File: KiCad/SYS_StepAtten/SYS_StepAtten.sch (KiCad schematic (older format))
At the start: 125 parts, among them J1 RCA-1, J2 RCA-2, J3 AUX-1-2, J4 Barrel_Jack 9Vac, J5 POT_EXT Conn, J6 cfg jumper, J7 ARM SWD, J8 RCA-Out, K1 TQ2SA, K10 TQ2SA, K11 TQ2SA, K12 TQ2SA, K13 TQ2SA, K14 TQ2SA, K2 TQ2SA, K3 TQ2SA, K4 TQ2SA, K5 TQ2SA, K6 TQ2SA, K7 TQ2SA, K8 TQ2SA, K9 TQ2SA, Q1 2N7002, Q10 2N7002, Q11 2N7002, Q12 2N7002, Q13 2N7002, Q14 2N7002, Q2 2N7002, Q3 2N7002, Q4 2N7002, Q5 2N7002, Q6 2N7002, Q7 2N7002, Q8 2N7002, Q9 2N7002, SW1 ON/OFF, SW2 INPUT_SWITCH, U1 LM317, U2 STM32f030K6T6, U3 L7805, Y1 8Mhz

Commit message: Cleared Annotations, Will have to redo pcb anyway
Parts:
- renumbered C13 to C?, C12 to C?, C5 to C?, C6 to C?, C2 to C?, C3 to C?, C14 to C?, C4 to C?, C10 to C?, C11 to C?, C9 to C?, C8 to C?, C7 to C?, C1 to C?, D11 to D?, D9 to D?, D10 to D?, D1 to D?, D7 to D?, D8 to D?, D2 to D?, D6 to D?, D12 to D?, D13 to D?, D14 to D?, D15 to D?, D16 to D?, D17 to D?, D18 to D?, D19 to D?, D20 to D?, D21 to D?, D3 to D?, D4 to D?, D5 to D?, H1 to H?, H2 to H?, J7 to J?, J3 to J?, J4 to J?, J6 to J?, J1 to J?, J2 to J?, J8 to J?, J5 to J?, JP1 to JP?, JP2 to JP?, K1 to K?, K2 to K?, K3 to K?, K4 to K?, K5 to K?, K6 to K?, K7 to K?, K8 to K?, K9 to K?, K10 to K?, K11 to K?, K12 to K?, K13 to K?, K14 to K?, Q4 to Q?, Q2 to Q?, Q3 to Q?, Q1 to Q?, Q6 to Q?, Q5 to Q?, Q8 to Q?, Q7 to Q?, Q10 to Q?, Q9 to Q?, Q12 to Q?, Q11 to Q?, Q14 to Q?, Q13 to Q?, R10 to R?, R9 to R?, R7 to R?, R8 to R?, R14 to R?, R13 to R?, R11 to R?, R12 to R?, R19 to R?, R18 to R?, R16 to R?, R17 to R?, R23 to R?, R22 to R?, R20 to R?, R21 to R?, R27 to R?, R26 to R?, R24 to R?, R25 to R?, R31 to R?, R30 to R?, R28 to R?, R29 to R?, R35 to R?, R34 to R?, R32 to R?, R33 to R?, R37 to R?, R36 to R?, R38 to R?, R39 to R?, R40 to R?, R41 to R?, R5 to R?, R6 to R?, R15 to R?, R2 to R?, R3 to R?, R4 to R?, R1 to R?, RV1 to RV?, SW1 to SW?, SW2 to SW?, TP1 to TP?, TP2 to TP?, U3 to U?, U1 to U?, U2 to U?, Y1 to Y?

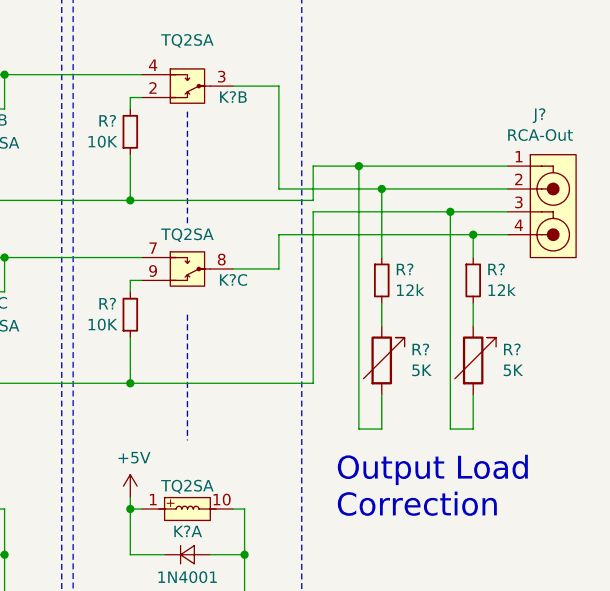
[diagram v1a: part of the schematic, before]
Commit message: Added Series Output Load Adjustment
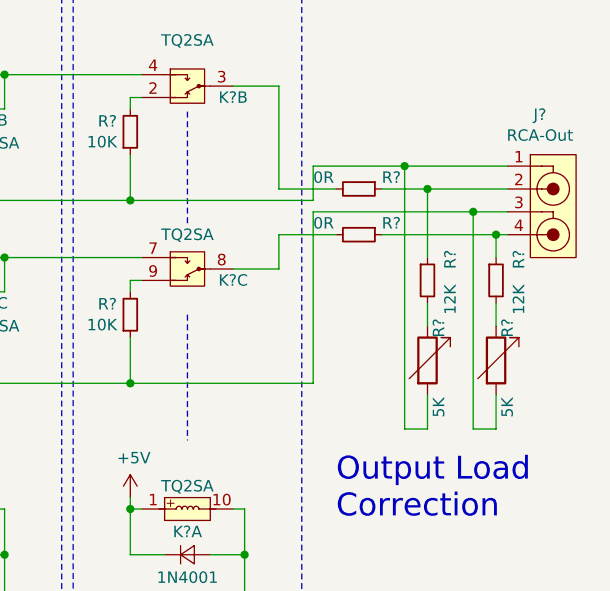
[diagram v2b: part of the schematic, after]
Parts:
- added R? (x2): 0R, Resistor_SMD:R_0603_1608Metric, symbol Device:R_Small
- R? (x2): value 12k -> 12K
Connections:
- net at J?.2, R?.1: now also R?.1; no longer K?.3
- net at J?.4, R?.1: now also R?.1; no longer K?.8
- new net: K?.8, R?.2
- new net: K?.3, R?.2
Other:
- moved on the sheet: R?
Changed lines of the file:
@@
 	1    0    0    -1
 $EndComp
-Wire Wire Line
-	14750 2450 15350 2450
-Wire Wire Line
-	14600 2550 15450 2550
 $Comp
 L Device:R_Small R?
 U 1 1 5F1C9E77
-P 15050 2750
-F 0 "R?" H 15109 2796 50  0000 L CNN
-F 1 "12k" H 15109 2705 50  0000 L CNN
-F 2 "Resistor_SMD:R_0603_1608Metric" H 15050 2750 50  0001 C CNN
-F 3 "~" H 15050 2750 50  0001 C CNN
-	1    15050 2750
+P 15250 2750
+F 0 "R?" V 15350 2800 50  0000 L CNN
+F 1 "12K" V 15350 2600 50  0000 L CNN
+F 2 "Resistor_SMD:R_0603_1608Metric" H 15250 2750 50  0001 C CNN
+F 3 "~" H 15250 2750 50  0001 C CNN
+	1    15250 2750
 	1    0    0    -1
 $EndComp
@@
 L Device:R_Variable R?
 U 1 1 5F1CB0BC
-P 15050 3100
-F 0 "R?" H 15178 3146 50  0000 L CNN
-F 1 "5K" H 15178 3055 50  0000 L CNN
-F 2 "Potentiometer_THT:Potentiometer_Bourns_3296W_Vertical" V 14980 3100 50  0001 C CNN
-F 3 "~" H 15050 3100 50  0001 C CNN
-	1    15050 3100
+P 15250 3100
+F 0 "R?" V 15300 3200 50  0000 L CNN
+F 1 "5K" V 15300 2850 50  0000 L CNN
+F 2 "Potentiometer_THT:Potentiometer_Bourns_3296W_Vertical" V 15180 3100 50  0001 C CNN
+F 3 "~" H 15250 3100 50  0001 C CNN
+	1    15250 3100
 	1    0    0    -1
 $EndComp
@@
 L Device:R_Small R?
 U 1 1 5F1CB5A8
-P 15450 2750
-F 0 "R?" H 15509 2796 50  0000 L CNN
-F 1 "12k" H 15509 2705 50  0000 L CNN
-F 2 "Resistor_SMD:R_0603_1608Metric" H 15450 2750 50  0001 C CNN
-F 3 "~" H 15450 2750 50  0001 C CNN
-	1    15450 2750
+P 15550 2750
+F 0 "R?" V 15650 2800 50  0000 L CNN
+F 1 "12K" V 15650 2600 50  0000 L CNN
+F 2 "Resistor_SMD:R_0603_1608Metric" H 15550 2750 50  0001 C CNN
+F 3 "~" H 15550 2750 50  0001 C CNN
+	1    15550 2750
 	1    0    0    -1
 $EndComp
@@
 L Device:R_Variable R?
 U 1 1 5F1F1DD1
-P 15450 3100
-F 0 "R?" H 15578 3146 50  0000 L CNN
-F 1 "5K" H 15578 3055 50  0000 L CNN
-F 2 "Potentiometer_THT:Potentiometer_Bourns_3296W_Vertical" V 15380 3100 50  0001 C CNN
-F 3 "~" H 15450 3100 50  0001 C CNN
-	1    15450 3100
+P 15550 3100
+F 0 "R?" V 15600 3200 50  0000 L CNN
+F 1 "5K" V 15600 2850 50  0000 L CNN
+F 2 "Potentiometer_THT:Potentiometer_Bourns_3296W_Vertical" V 15480 3100 50  0001 C CNN
+F 3 "~" H 15550 3100 50  0001 C CNN
+	1    15550 3100
 	1    0    0    -1
 $EndComp
 Wire Wire Line
-	15450 2950 15450 2850
-Wire Wire Line
-	15050 2850 15050 2950
-Wire Wire Line
-	15450 2650 15450 2550
-Connection ~ 15450 2550
+	15550 2950 15550 2850
 Wire Wire Line
-	15450 2550 15600 2550
+	15250 2850 15250 2950
 Wire Wire Line
-	15050 2650 15050 2350
+	15550 2650 15550 2550
 Wire Wire Line
-	15050 2350 15600 2350
+	15250 2650 15250 2350
 Wire Wire Line
-	15050 3250 15050 3400
+	15250 3250 15250 3400
 Wire Wire Line
-	15050 3400 14950 3400
+	15250 3400 15150 3400
 Wire Wire Line
-	14950 3400 14950 2250
+	15150 3400 15150 2250
 Wire Wire Line
-	14950 2250 15600 2250
+	15550 3250 15550 3400
 Wire Wire Line
-	15450 3250 15450 3400
+	15550 3400 15450 3400
 Wire Wire Line
-	15450 3400 15350 3400
-Wire Wire Line
-	15350 3400 15350 2450
-Connection ~ 15350 2450
-Wire Wire Line
-	15350 2450 15600 2450
+	15450 3400 15450 2450
 $Comp
 L Connector_Generic:Conn_02x05_Odd_Even J?
@@
 $EndComp
 Wire Wire Line
-	14750 2250 14950 2250
-Wire Wire Line
 	14750 2250 14750 2400
-Connection ~ 14950 2250
-Wire Wire Line
-	15050 2350 14600 2350
 Wire Wire Line
 	14600 1900 14600 2350
-Connection ~ 15050 2350
+$Comp
+L Device:R_Small R?
+U 1 1 5EF195F1
+P 14950 2550
+F 0 "R?" V 14900 2650 50  0000 L CNN
+F 1 "0R" V 14900 2350 50  0000 L CNN
+F 2 "Resistor_SMD:R_0603_1608Metric" H 14950 2550 50  0001 C CNN
+F 3 "~" H 14950 2550 50  0001 C CNN
+	1    14950 2550
+	0    1    1    0
+$EndComp
+$Comp
+L Device:R_Small R?
+U 1 1 5F00084E
+P 14950 2350
+F 0 "R?" V 14900 2450 50  0000 L CNN
+F 1 "0R" V 14900 2150 50  0000 L CNN
+F 2 "Resistor_SMD:R_0603_1608Metric" H 14950 2350 50  0001 C CNN
+F 3 "~" H 14950 2350 50  0001 C CNN
+	1    14950 2350
+	0    1    1    0
+$EndComp
+Wire Wire Line
+	14850 2350 14600 2350
+Wire Wire Line
+	15050 2350 15250 2350
+Wire Wire Line
+	15250 2350 15600 2350
+Connection ~ 15250 2350
+Wire Wire Line
+	15600 2250 15150 2250
+Wire Wire Line
+	15150 2250 14750 2250
+Connection ~ 15150 2250
+Wire Wire Line
+	15050 2550 15550 2550
+Wire Wire Line
+	15550 2550 15600 2550
+Connection ~ 15550 2550
+Wire Wire Line
+	15450 2450 15600 2450
+Wire Wire Line
+	15450 2450 14750 2450
+Connection ~ 15450 2450
+Wire Wire Line
+	14600 2550 14850 2550
 $EndSCHEMATC

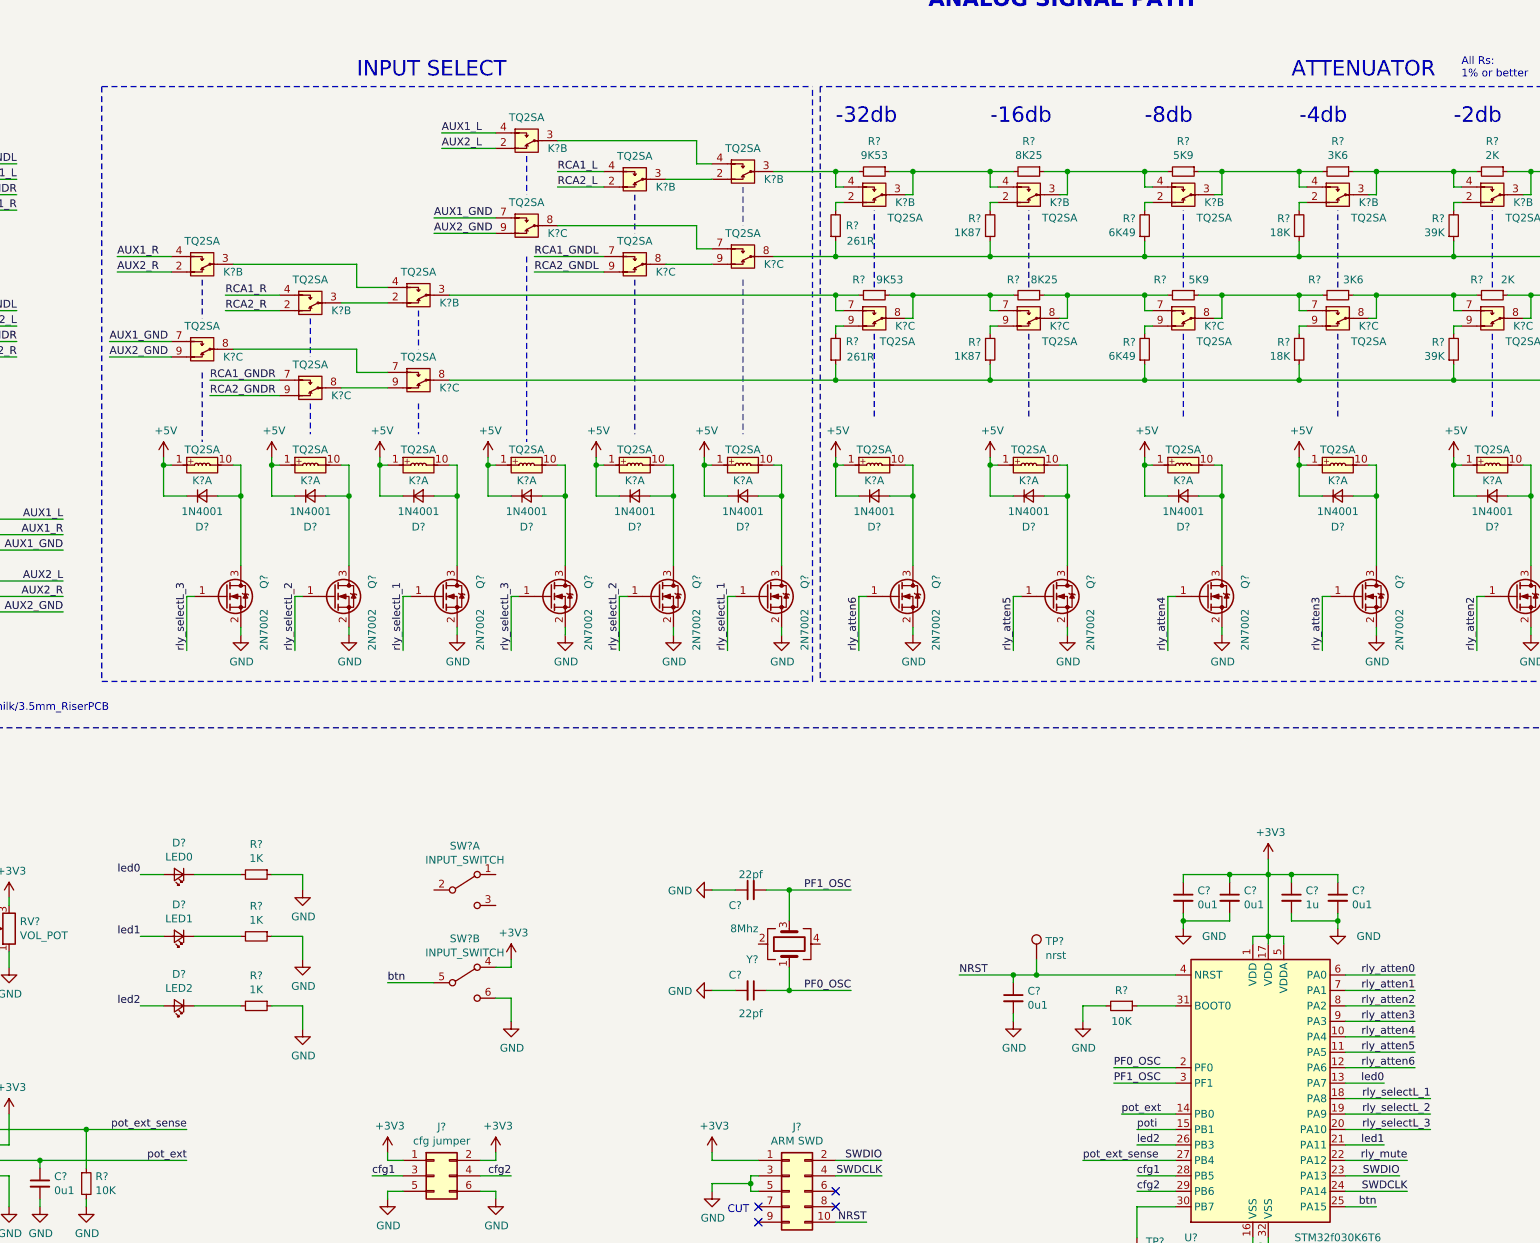
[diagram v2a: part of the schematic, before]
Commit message: Reassigned Selection Relays
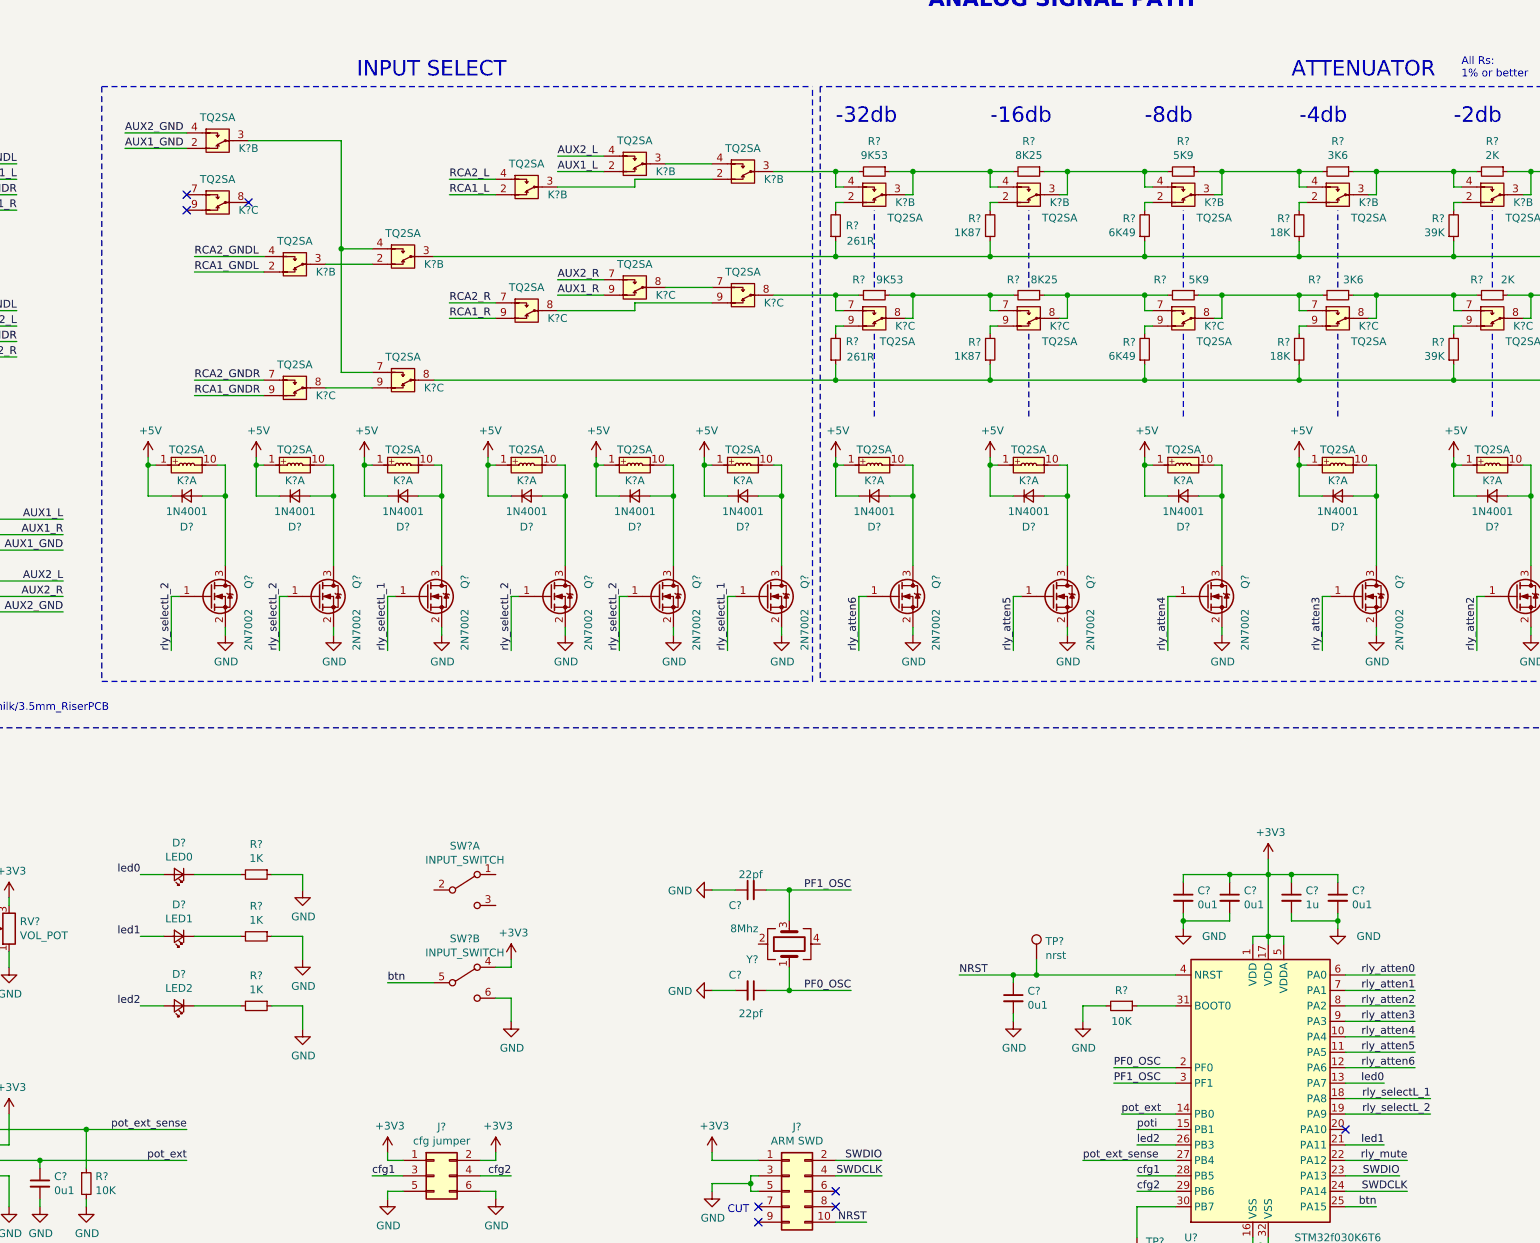
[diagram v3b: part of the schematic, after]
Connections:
- net AUX1_GND: now also K?.2; no longer K?.7, K?.7
- net AUX1_L: now also K?.2; no longer K?.4
- net AUX1_R: now also K?.9; no longer K?.4
- net AUX2_GND: now also K?.4; no longer K?.9, K?.9
- net AUX2_L: now also K?.4; no longer K?.2
- net AUX2_R: now also K?.7; no longer K?.2
- net RCA1_GNDL: now also K?.2; no longer K?.7
- net RCA1_GNDR: now also K?.9; no longer K?.7
- net RCA1_L: now also K?.2; no longer K?.4
- net RCA1_R: now also K?.9; no longer K?.4
- net RCA2_GNDL: now also K?.4; no longer K?.9
- net RCA2_GNDR: now also K?.7; no longer K?.9
- net RCA2_L: now also K?.4; no longer K?.2
- net RCA2_R: now also K?.7; no longer K?.2
- net rly_selectL_2: now also Q?.1 (G), Q?.1 (G)
- net at K?.7, R?.2: now also K?.8; no longer K?.3
- net at J?.1, R?.1, R?.1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: now also K?.3; no longer K?.8
- net at K?.8: no longer K?.7
- net at K?.3, K?.4: now also K?.7
- net at K?.3: now also K?.2; no longer K?.4
- net at K?.8: now also K?.9; no longer K?.7
- net at K?.3: now also K?.4; no longer K?.2
- net at K?.8: now also K?.7; no longer K?.9
- removed net rly_selectL_3: Q?.1 (G), Q?.1 (G), U?.20 (PA10)
- no-connect marks 4 -> 8
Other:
- moved on the sheet: D?, K?A, K?B, K?C, Q?

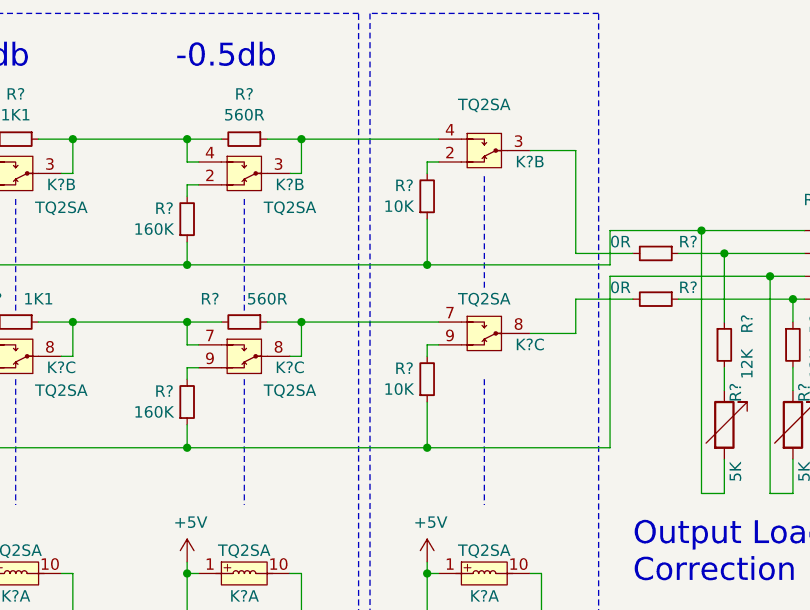
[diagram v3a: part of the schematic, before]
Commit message: Changed Mute to be short
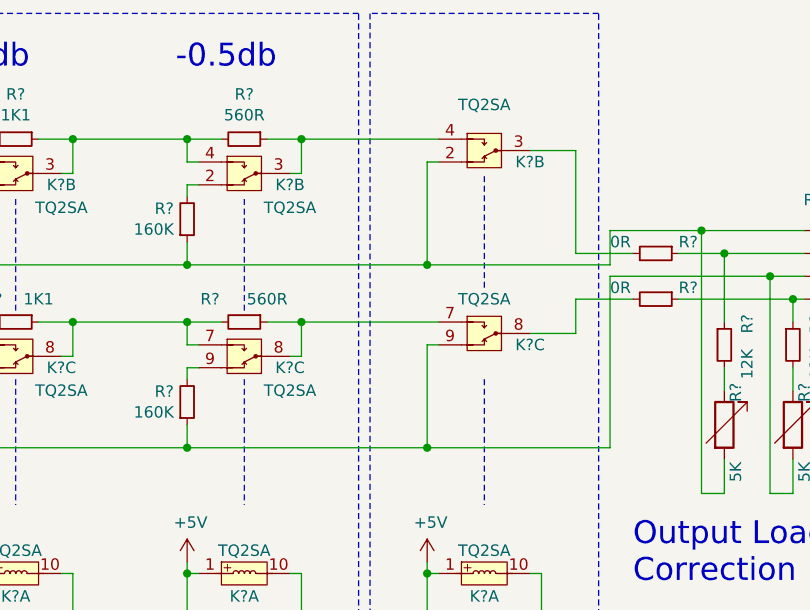
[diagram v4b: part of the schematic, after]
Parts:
- removed R? (x2): 10K, Resistor_SMD:R_0603_1608Metric, symbol Device:R_Small
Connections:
- net at J?.1, K?.3, R?.1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: now also K?.2
- net at J?.3, K?.8, R?.1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: now also K?.9
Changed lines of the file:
@@
 Wire Wire Line
 	12900 2850 12900 2900
-$Comp
-L Device:R_Small R?
-U 1 1 5EA3E21B
-P 13950 2900
-F 0 "R?" H 13892 2854 50  0000 R CNN
-F 1 "10K" H 13892 2945 50  0000 R CNN
-F 2 "Resistor_SMD:R_0603_1608Metric" H 13950 2900 50  0001 C CNN
-F 3 "~" H 13950 2900 50  0001 C CNN
-	1    13950 2900
-	1    0    0    1
-$EndComp
 Wire Wire Line
 	14000 2750 13950 2750
 Wire Wire Line
-	13950 2750 13950 2800
-$Comp
-L Device:R_Small R?
-U 1 1 5EA43546
-P 13950 2100
-F 0 "R?" H 13892 2054 50  0000 R CNN
-F 1 "10K" H 13892 2145 50  0000 R CNN
-F 2 "Resistor_SMD:R_0603_1608Metric" H 13950 2100 50  0001 C CNN
-F 3 "~" H 13950 2100 50  0001 C CNN
-	1    13950 2100
-	1    0    0    1
-$EndComp
-Wire Wire Line
 	14000 1950 13950 1950
-Wire Wire Line
-	13950 1950 13950 2000
 Text Notes 9850 1250 0    100  ~ 0
 ATTENUATOR
@@
 	7900 3200 8900 3200
 Wire Wire Line
-	13950 3000 13950 3200
-Wire Wire Line
-	13950 2200 13950 2400
-Wire Wire Line
 	12900 2400 11900 2400
 Wire Wire Line
@@
 $EndComp
 NoConn ~ 10200 8050
+Wire Wire Line
+	13950 1950 13950 2400
+Wire Wire Line
+	13950 2750 13950 3200
 $EndSCHEMATC
